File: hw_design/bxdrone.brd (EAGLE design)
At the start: 72.3 x 69.9 mm, 23 parts, among them J1 POWER_JACKPTH_BREAD

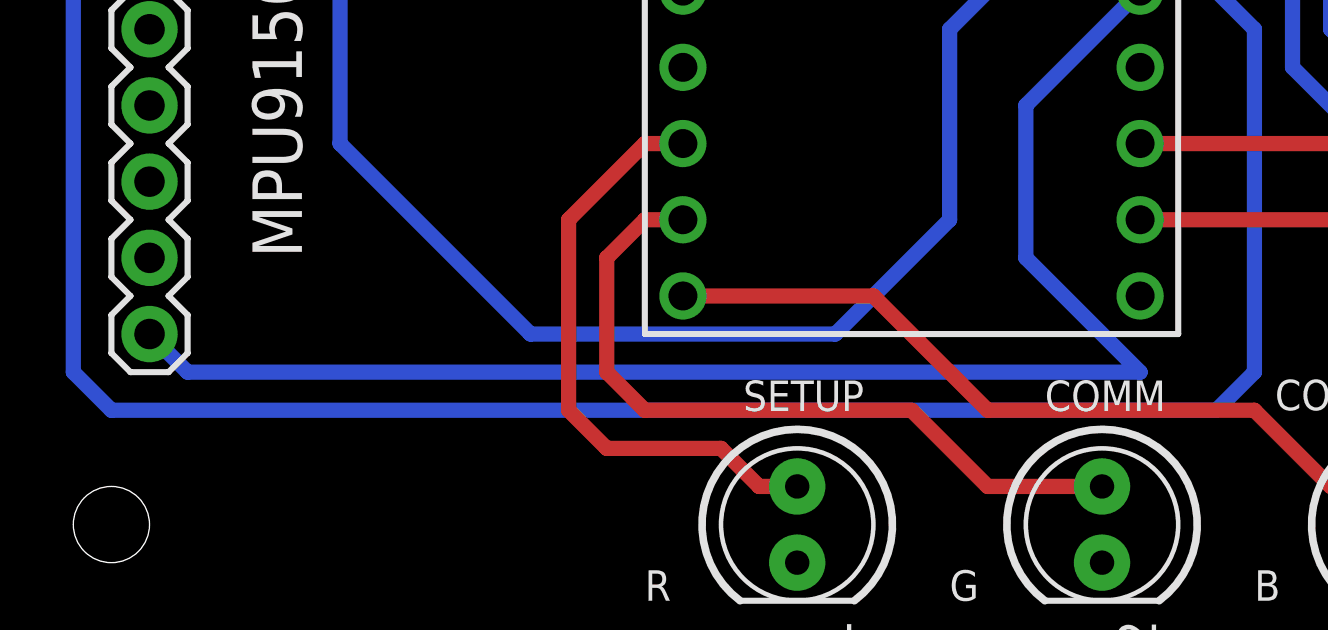
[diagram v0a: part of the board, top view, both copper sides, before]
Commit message: Modified one of the tracks on the bottom side
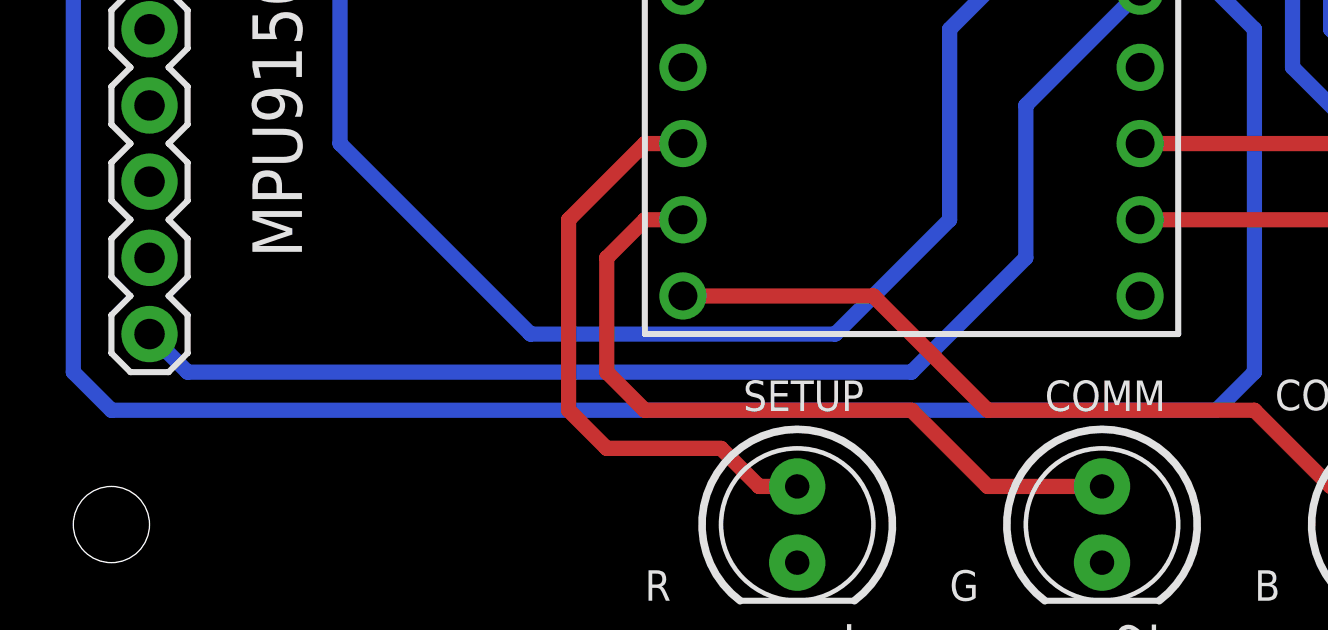
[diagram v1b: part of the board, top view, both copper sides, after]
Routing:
- net INT: track 49.4 -> 41.8 mm
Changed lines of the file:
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@@
 <grid distance="0.05" unitdist="inch" unit="inch" style="lines" multiple="1" display="yes" altdistance="0.001" altunitdist="inch" altunit="inch"/>
 <layers>
-<layer number="1" name="Top" color="4" fill="1" visible="yes" active="yes"/>
-<layer number="16" name="Bottom" color="1" fill="1" visible="no" active="yes"/>
+<layer number="1" name="Top" color="4" fill="1" visible="no" active="yes"/>
+<layer number="16" name="Bottom" color="1" fill="1" visible="yes" active="yes"/>
 <layer number="17" name="Pads" color="2" fill="1" visible="yes" active="yes"/>
 <layer number="18" name="Vias" color="2" fill="1" visible="yes" active="yes"/>
-<layer number="19" name="Unrouted" color="6" fill="1" visible="no" active="yes"/>
+<layer number="19" name="Unrouted" color="6" fill="1" visible="yes" active="yes"/>
 <layer number="20" name="Dimension" color="15" fill="1" visible="yes" active="yes"/>
 <layer number="21" name="tPlace" color="7" fill="1" visible="yes" active="yes"/>
@@
 <contactref element="J2" pad="11"/>
 <contactref element="U$2" pad="17/A3"/>
-<wire x1="6.35" y1="8.89" x2="38.1" y2="8.89" width="0.508" layer="16"/>
-<wire x1="38.1" y1="8.89" x2="34.29" y2="12.7" width="0.508" layer="16"/>
 <wire x1="34.29" y1="12.7" x2="34.29" y2="17.78" width="0.508" layer="16"/>
 <wire x1="34.29" y1="17.78" x2="38.1" y2="21.59" width="0.508" layer="16"/>
 <wire x1="6.35" y1="8.89" x2="5.08" y2="10.16" width="0.508" layer="16"/>
+<wire x1="34.29" y1="12.7" x2="30.48" y2="8.89" width="0.508" layer="16"/>
+<wire x1="30.48" y1="8.89" x2="6.35" y2="8.89" width="0.508" layer="16"/>
 </signal>
 <signal name="M1">

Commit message: Starting to change board design
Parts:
- moved J9 70.6 mm to (64.8, 6.35), turned to 0 degrees
- moved J1 69.9 mm to (30.5, 2.54), turned to 0 degrees
- moved C1 68.4 mm to (54.6, 6.35)
- moved J7 63.8 mm to (22.9, 66.0), turned to 0 degrees
- moved SW_5V 58.5 mm to (47.0, 8.89)
- moved R1 56.1 mm to (5.08, 62.2)
- moved R2 56.1 mm to (8.89, 62.2)
- moved SW_3V3 53.9 mm to (40.6, 8.89), turned to 0 degrees
- moved D1 49.8 mm to (66.0, 34.3), turned to 0 degrees
- moved J8 44.9 mm to (35.6, 66.0), turned to 0 degrees
- moved J3 40.8 mm to (21.6, 7.62), turned to 90 degrees
- moved J4 40.8 mm to (19.1, 7.62), turned to 90 degrees
- moved J5 40.8 mm to (8.89, 7.62), turned to 90 degrees
- moved J6 40.8 mm to (6.35, 7.62), turned to 90 degrees
- moved 3V3_REG 36.1 mm to (53.3, 26.7), turned to 180 degrees
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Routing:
- net TX: track 100.7 -> 0.00 mm
- net REDLED: track 19.9 -> 101.7 mm
- net SDA: track 80.6 -> 0.00 mm
- net RX: track 74.5 -> 0.00 mm
- net GND: track 118.7 -> 45.6 mm
- net GREENLED: track 25.0 -> 84.4 mm
- net BLUELED: track 26.8 -> 85.3 mm
- net SCL: track 56.2 -> 0.00 mm
- net +5V: track 41.9 -> 97.2 mm
- net RX_STATE: track 55.1 -> 0.00 mm
- net INT: track 41.8 -> 0.00 mm
- net TX_STATE: track 38.5 -> 0.00 mm
- net +3V3: track 113.6 -> 78.3 mm
- net +12V: track 29.6 -> 62.7 mm
- net M1: track 11.7 -> 36.8 mm
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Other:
- board size 72.3 x 69.9 mm -> 184.2 x 69.8 mm

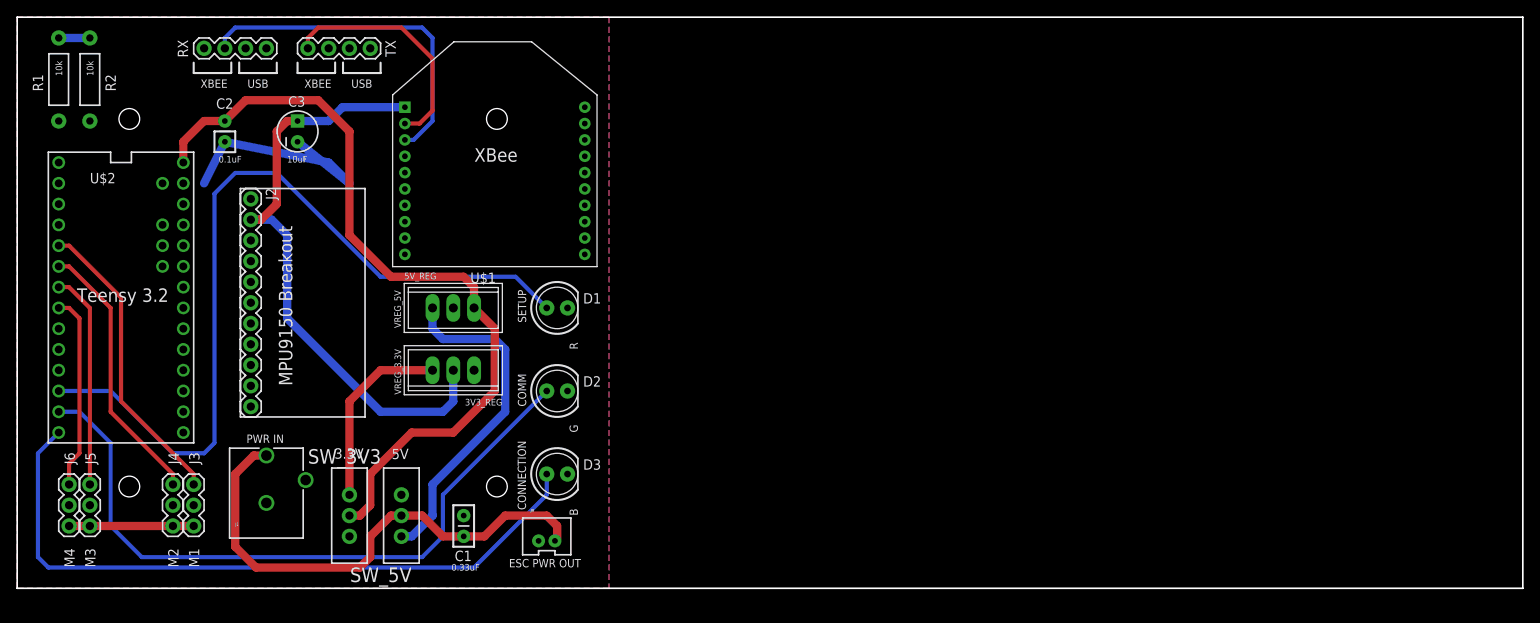
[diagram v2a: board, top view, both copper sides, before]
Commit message: Finished board rearrangement
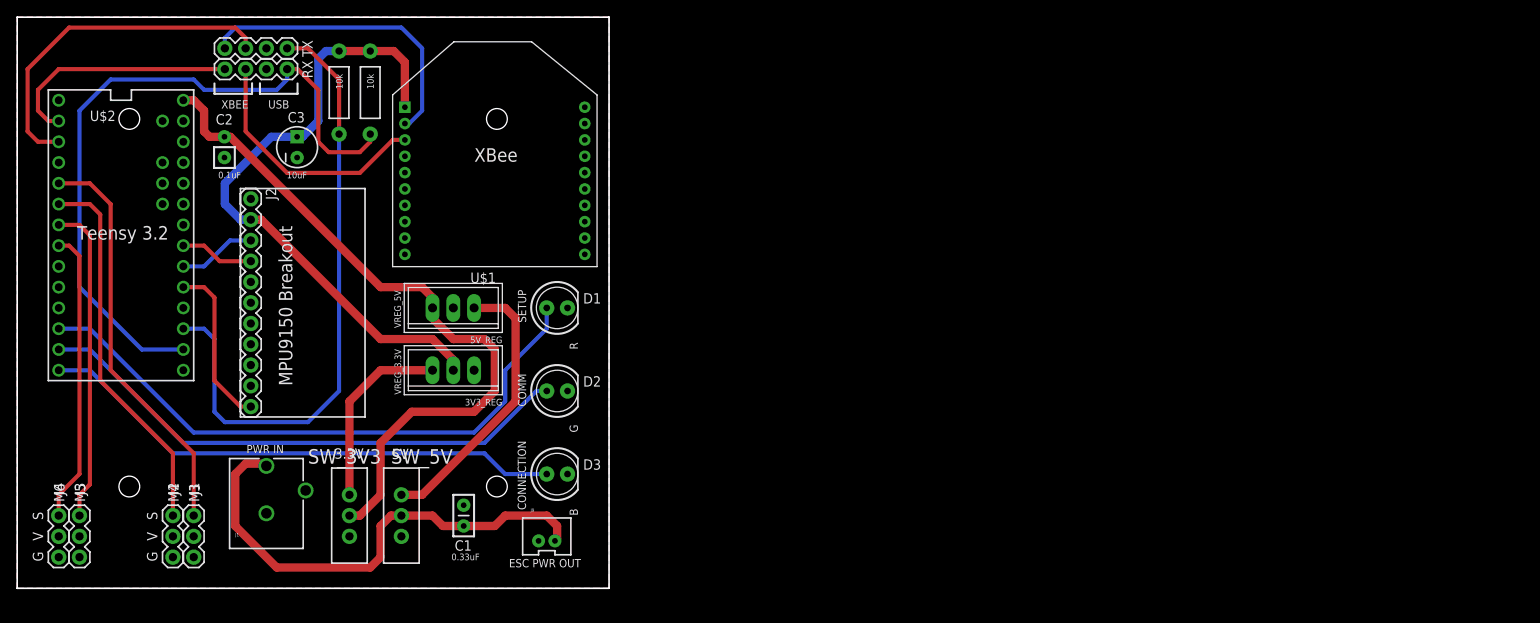
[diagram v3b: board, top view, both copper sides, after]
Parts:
- moved R1 34.3 mm to (39.4, 60.6)
- moved R2 34.3 mm to (43.2, 60.6)
- moved J8 10.2 mm to (25.4, 66.0)
- moved U$2 7.62 mm to (12.7, 43.2)
- moved J5 4.02 mm to (7.62, 3.81)
- moved J6 4.02 mm to (5.08, 3.81)
- moved J3 3.81 mm to (21.6, 3.81)
- moved J4 3.81 mm to (19.1, 3.81)
- moved J7 3.59 mm to (25.4, 63.5)
- moved C3 1.93 mm to (34.2, 53.9)
- moved C2 1.93 mm to (25.3, 55.2)
- moved C1 1.27 mm to (54.6, 7.62)
- moved J1 1.27 mm to (30.5, 1.27)
- turned 5V_REG to 180 degrees
- turned SW_5V to 0 degrees
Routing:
- net RX_STATE: track 0.00 -> 86.3 mm
- net TX_STATE: track 0.00 -> 76.6 mm
- net GND: track 45.6 -> 0.00 mm
- net TX: track 0.00 -> 42.5 mm
- net RX: track 0.00 -> 29.5 mm
- net REDLED: track 101.7 -> 75.0 mm
- net BLUELED: track 85.3 -> 65.0 mm
- net INT: track 0.00 -> 20.3 mm
- net GREENLED: track 84.4 -> 67.1 mm
- net M1: track 36.8 -> 49.7 mm
- net M2: track 33.2 -> 46.1 mm
- net M3: track 26.5 -> 39.2 mm
- net M4: track 23.9 -> 35.9 mm
- net XBEE_RX: track 42.2 -> 30.9 mm
- net +5V: track 97.2 -> 86.6 mm
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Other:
- board size 184.2 x 69.8 mm -> 72.4 x 69.8 mm
- board text added: "S"
- board text added: "V"

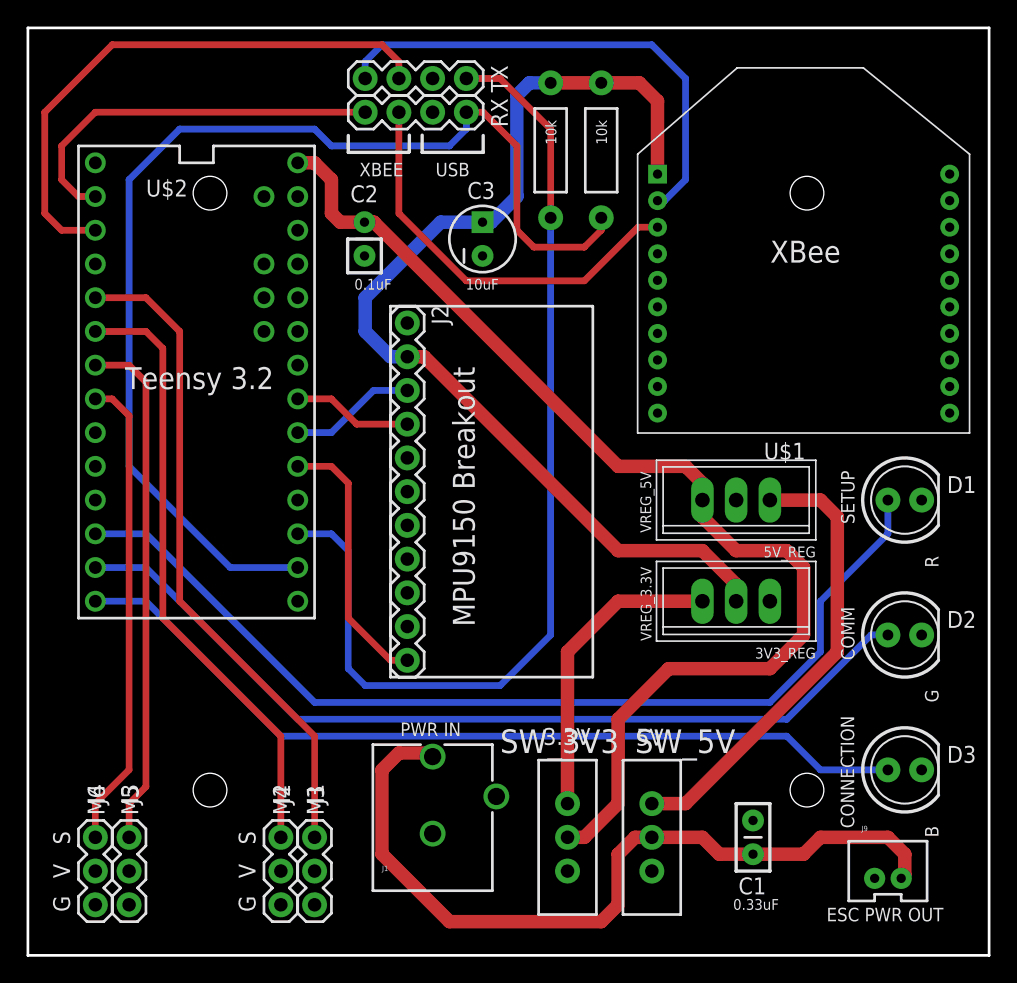
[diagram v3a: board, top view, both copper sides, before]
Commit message: Changed connection with XBee and holes positions in board
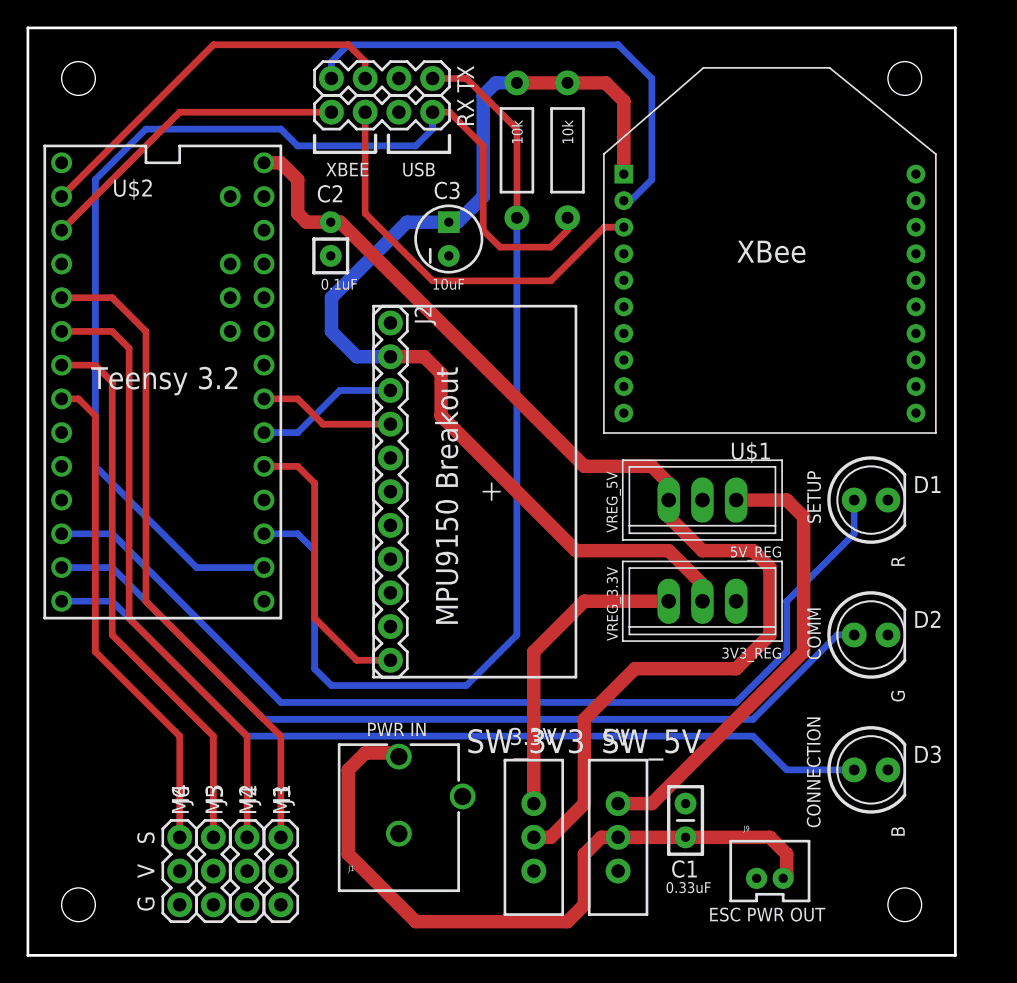
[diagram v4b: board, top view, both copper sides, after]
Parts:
- moved J9 8.89 mm to (55.9, 6.35)
- moved J5 6.35 mm to (14.0, 3.81)
- moved J6 6.35 mm to (11.4, 3.81)
- moved C1 5.24 mm to (49.5, 8.89)
- moved 3V3_REG 2.54 mm to (50.8, 26.7)
- moved 5V_REG 2.54 mm to (50.8, 34.3)
- moved D1 2.54 mm to (63.5, 34.3)
- moved D2 2.54 mm to (63.5, 24.1)
- moved D3 2.54 mm to (63.5, 14.0)
- moved C2 2.54 mm to (22.8, 55.2)
- moved J1 2.54 mm to (27.9, 1.27)
- moved J3 2.54 mm to (19.1, 3.81)
- moved J4 2.54 mm to (16.5, 3.81)
- moved J7 2.54 mm to (22.9, 63.5)
- moved J8 2.54 mm to (22.9, 66.0)
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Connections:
- net RX: now also J8.2; no longer J7.1
- net TX: now also J7.1; no longer J8.2
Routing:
- net TX: track 42.5 -> 24.0 mm
- net +12V: track 60.6 -> 53.2 mm
- net M3: track 39.2 -> 41.8 mm
- net +3V3: track 78.9 -> 80.8 mm
- net M4: track 35.9 -> 37.4 mm
- net SDA: track 9.57 -> 10.8 mm
- net SCL: track 9.04 -> 10.3 mm
- net INT: track 20.3 -> 21.5 mm
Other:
- board size 72.4 x 69.8 mm -> 69.8 x 69.8 mm
